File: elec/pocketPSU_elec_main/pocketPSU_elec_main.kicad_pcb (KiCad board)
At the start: 2 copper layers, 90 x 90 mm, 72 parts, among them J1 Conn_01x20_Pin, J2 Conn_01x03_Pin, J3 Conn_01x12_Pin, SW1 EC11E09244BS, SW3 TS-1187A-B-A-B, SW6 TS-1187A-B-A-B, U1 2N7002_C5224215, U2 ESP32-S3-WROOM-1(N16R2), U3 AMS1117-3.3, U4 FUSB302MPX, U5 F.0603.00026/P2-0603B1TS2-06T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

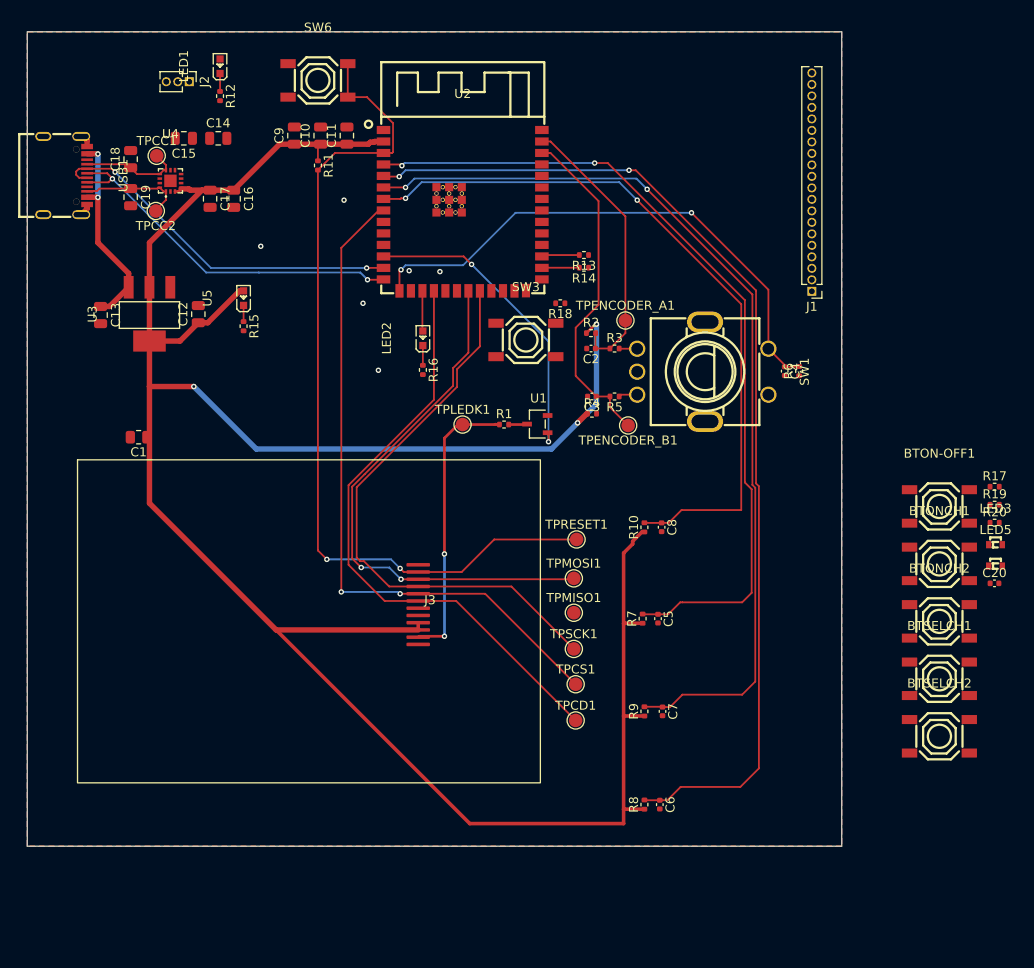
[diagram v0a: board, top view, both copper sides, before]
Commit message: move components, add mounting holes
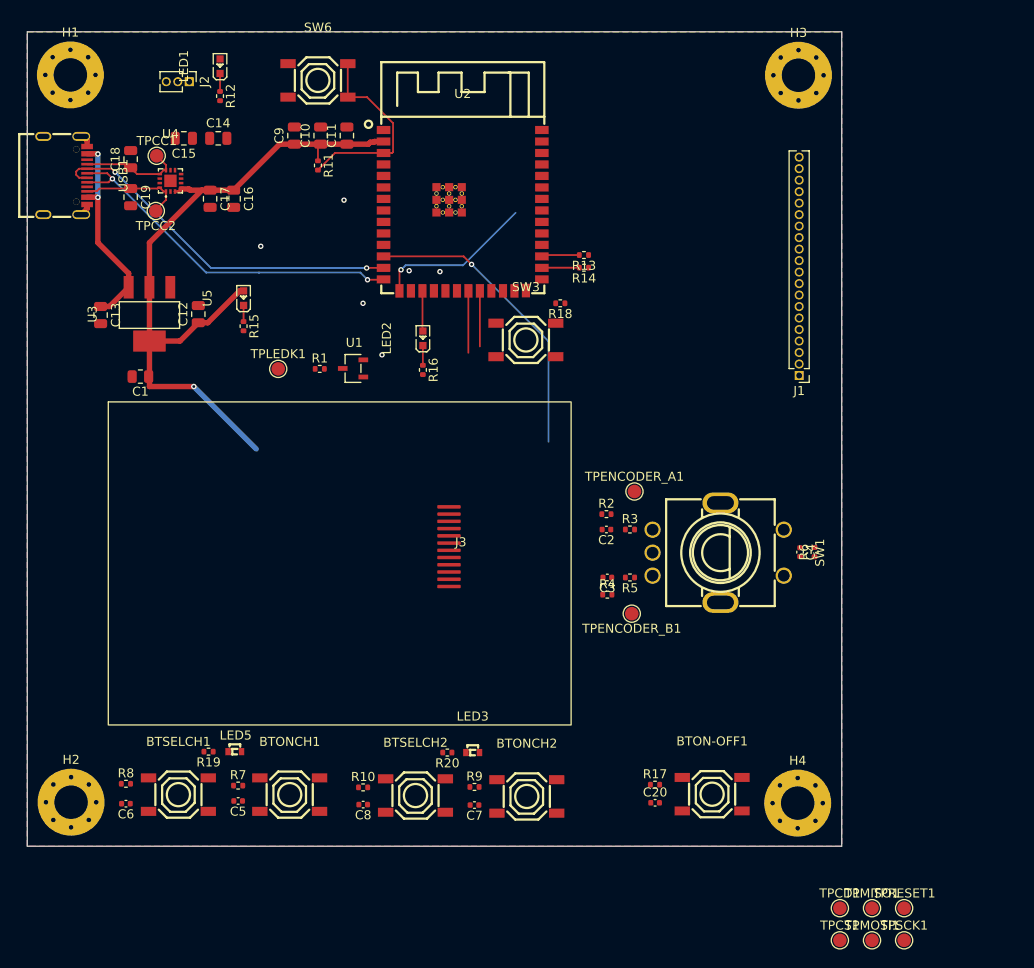
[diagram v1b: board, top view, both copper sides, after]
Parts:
- added H1: MountingHole, MountingHole:MountingHole_3.7mm_Pad_Via, F.Cu at (102.4, 40.5)
- added H2: MountingHole, MountingHole:MountingHole_3.7mm_Pad_Via, F.Cu at (102.4, 120.8)
- added H3: MountingHole, MountingHole:MountingHole_3.7mm_Pad_Via, F.Cu at (182.8, 40.5)
- added H4: MountingHole, MountingHole:MountingHole_3.7mm_Pad_Via, F.Cu at (182.7, 120.9)
- moved R19 91.1 mm to (117.6, 115.2), turned to 180 degrees
- moved LED5 86.5 mm to (120.5, 115.2)
- moved BTSELCH1 85.1 mm to (114.3, 120.0)
- moved BTONCH1 76.2 mm to (126.6, 120.0)
- moved R20 65.6 mm to (144.0, 115.3), turned to 180 degrees
- moved LED3 62.2 mm to (146.8, 115.3)
- moved C6 59.0 mm to (108.5, 121.0), turned to 180 degrees
- moved BTSELCH2 58.3 mm to (140.5, 120.1)
- moved R8 57.3 mm to (108.5, 118.8), turned to 0 degrees
- moved TPRESET1 54.5 mm to (194.5, 132.6)
- moved TPMOSI1 51.8 mm to (190.9, 136.1)
- moved C5 50.6 mm to (120.9, 120.7), turned to 180 degrees
- moved R17 49.9 mm to (167.0, 118.9)
- moved BTONCH2 49.5 mm to (152.8, 120.2)
- moved TPSCK1 48.7 mm to (194.5, 136.1)
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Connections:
- BTON-OFF1 pad 1: /microcontroller/BT_ON_CH2 -> /microcontroller/BT_ON_OFF
- BTON-OFF1 pad 2: /microcontroller/BT_ON_CH2 -> /microcontroller/BT_ON_OFF
- BTSELCH1 pad 1: /microcontroller/BT_ON_OFF -> /microcontroller/BT_ON_CH2
- BTSELCH1 pad 2: /microcontroller/BT_ON_OFF -> /microcontroller/BT_ON_CH2
- C20 pad 1: /microcontroller/BT_ON_CH2 -> /microcontroller/BT_ON_OFF
- C6 pad 1: /microcontroller/BT_ON_OFF -> /microcontroller/BT_ON_CH2
- R17 pad 2: /microcontroller/BT_ON_CH2 -> /microcontroller/BT_ON_OFF
- R8 pad 2: /microcontroller/BT_ON_OFF -> /microcontroller/BT_ON_CH2
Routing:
- net (no net): track 194.0 -> 0.00 mm, vias 4 -> 0
- net +3.3V: track 266.9 -> 78.9 mm, vias 3 -> 1
- net /microcontroller/BT_SEL_CH2: track 102.8 -> 0.00 mm, vias 2 -> 0
- net /microcontroller/BT_SEL_CH1: track 92.1 -> 0.00 mm, vias 2 -> 0
- net /user_interface/SPI_CS: track 74.5 -> 0.53 mm, vias 2 -> 0
- net /user_interface/SPI_RESET: track 95.3 -> 22.2 mm, vias 2 -> 0
- net /user_interface/SPI_DC: track 66.4 -> 0.00 mm
- net /user_interface/SPI_SCK: track 63.3 -> 6.14 mm
- net /user_interface/SPI_MOSI: track 60.4 -> 6.84 mm, vias 2 -> 0
- net /microcontroller/ENCODER_BT: track 60.0 -> 17.7 mm, vias 2 -> 1
- net /microcontroller/ENCODER_B: track 37.6 -> 0.00 mm
- net /user_interface/LEDK: track 31.6 -> 0.00 mm, vias 2 -> 0
- net /microcontroller/ENCODER_A: track 31.3 -> 0.00 mm
- net Net-(R5-Pad1): track 2.07 -> 0.00 mm
- net Net-(R3-Pad2): track 2.00 -> 0.00 mm
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
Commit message: board routed
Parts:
- J1: value Conn_01x20_Pin -> Header-Male-2.54_1x20; footprint Connector_PinHeader_1.27mm:PinHeader_1x20_P1.27mm_Vertical -> footprints:HDR-TH_20P-P2.54-V-M-1
- moved TPMISO1 79.3 mm to (144.9, 68.0)
- moved TPRESET1 61.4 mm to (160.1, 81.7)
- moved TPMOSI1 59.6 mm to (160.1, 85.1)
- moved TPSCK1 58.8 mm to (160.0, 88.5)
- moved TPCS1 51.9 mm to (159.9, 92.1)
- moved TPCD1 45.9 mm to (160.0, 95.7)
- moved R6 18.6 mm to (170.1, 104.8), turned to 0 degrees
- moved C4 16.4 mm to (170.1, 103.2), turned to 180 degrees
- moved R4 16.4 mm to (165.4, 82.0), turned to -90 degrees
- moved TPENCODER_B1 15.4 mm to (163.3, 84.7), turned to 90 degrees
- moved C3 15.1 mm to (167.3, 82.0), turned to 90 degrees
- moved R2 14.5 mm to (174.3, 81.8), turned to -90 degrees
- moved C2 14.1 mm to (172.6, 81.8), turned to 90 degrees
- moved TPENCODER_A1 12.2 mm to (176.8, 85.0), turned to -90 degrees
- moved R5 11.9 mm to (167.3, 84.5), turned to 90 degrees
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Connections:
- J1 pad 1: /microcontroller/IO17 -> unconnected-(J1-Pad1)
- J1 pad 10: /microcontroller/IO45 -> /microcontroller/IO46
- J1 pad 11: /microcontroller/IO46 -> /microcontroller/IO45
- J1 pad 12: /microcontroller/IO47 -> /microcontroller/IO42
- J1 pad 13: /microcontroller/IO48 -> /microcontroller/IO41
- J1 pad 14: /microcontroller/TXD0 -> /microcontroller/IO40
- J1 pad 15: /microcontroller/RXD0 -> /microcontroller/IO39
- J1 pad 16: unconnected-(J1-Pin_16-Pad16) -> /microcontroller/IO38
- J1 pad 17: unconnected-(J1-Pin_17-Pad17) -> /microcontroller/IO21
- J1 pad 18: unconnected-(J1-Pin_18-Pad18) -> /microcontroller/IO11
- J1 pad 19: unconnected-(J1-Pin_19-Pad19) -> /microcontroller/IO18
- J1 pad 2: /microcontroller/IO18 -> unconnected-(J1-Pad2)
- J1 pad 20: unconnected-(J1-Pin_20-Pad20) -> /microcontroller/IO17
- J1 pad 3: /microcontroller/IO11 -> unconnected-(J1-Pad3)
- J1 pad 4: /microcontroller/IO21 -> unconnected-(J1-Pad4)
- J1 pad 5: /microcontroller/IO38 -> unconnected-(J1-Pad5)
- J1 pad 6: /microcontroller/IO39 -> /microcontroller/RXD0
- J1 pad 7: /microcontroller/IO40 -> /microcontroller/TXD0
- J1 pad 8: /microcontroller/IO41 -> /microcontroller/IO48
- J1 pad 9: /microcontroller/IO42 -> /microcontroller/IO47
- R18 pad 2: Net-(SW3-B) -> Net-(SW3-A)
- R2 pad 2: /microcontroller/ENCODER_A -> Net-(R2-Pad2)
- R3 pad 2: Net-(R3-Pad2) -> Net-(R2-Pad2)
- R4 pad 2: /microcontroller/ENCODER_B -> Net-(R4-Pad2)
- R5 pad 1: Net-(R5-Pad1) -> Net-(R4-Pad2)
- SW1 pad A: Net-(R3-Pad2) -> Net-(R2-Pad2)
- SW1 pad B: Net-(R5-Pad1) -> Net-(R4-Pad2)
- SW3 pad 1: GND -> Net-(SW3-A)
- SW3 pad 2: Net-(SW3-B) -> Net-(SW3-A)
- SW3 pad 4: Net-(SW3-B) -> GND
- SW6 pad 1: GND -> /user_interface/SPI_RESET
- SW6 pad 4: /user_interface/SPI_RESET -> GND
- U2 pad 27: Net-(SW3-B) -> Net-(SW3-A)
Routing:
- net +3.3V: track 78.9 -> 305.3 mm, vias 1 -> 10
- net /microcontroller/BT_ON_OFF: track 0.00 -> 106.7 mm, vias 0 -> 2
- net /user_interface/SPI_RESET: track 22.2 -> 118.2 mm, vias 0 -> 7
- net /microcontroller/BT_SEL_CH2: track 0.00 -> 93.7 mm
- net /microcontroller/BT_ON_CH2: track 0.00 -> 91.4 mm, vias 0 -> 2
- net /microcontroller/BT_ON_CH1: track 0.00 -> 88.3 mm
- net /microcontroller/BT_SEL_CH1: track 0.00 -> 87.0 mm
- net /microcontroller/CH2_LED: track 0.00 -> 76.0 mm, vias 0 -> 2
- net /user_interface/SPI_CS: track 0.53 -> 70.6 mm, vias 0 -> 6
- net /microcontroller/CH1_LED: track 0.00 -> 69.0 mm, vias 0 -> 2
- net /microcontroller/IO11: track 0.00 -> 65.5 mm, vias 0 -> 1
- net /microcontroller/ENCODER_A: track 0.00 -> 65.0 mm, vias 0 -> 2
- net /microcontroller/IO21: track 0.00 -> 61.5 mm, vias 0 -> 3
- net /microcontroller/ENCODER_B: track 0.00 -> 58.6 mm, vias 0 -> 2
- net /microcontroller/IO46: track 0.00 -> 57.5 mm, vias 0 -> 3
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
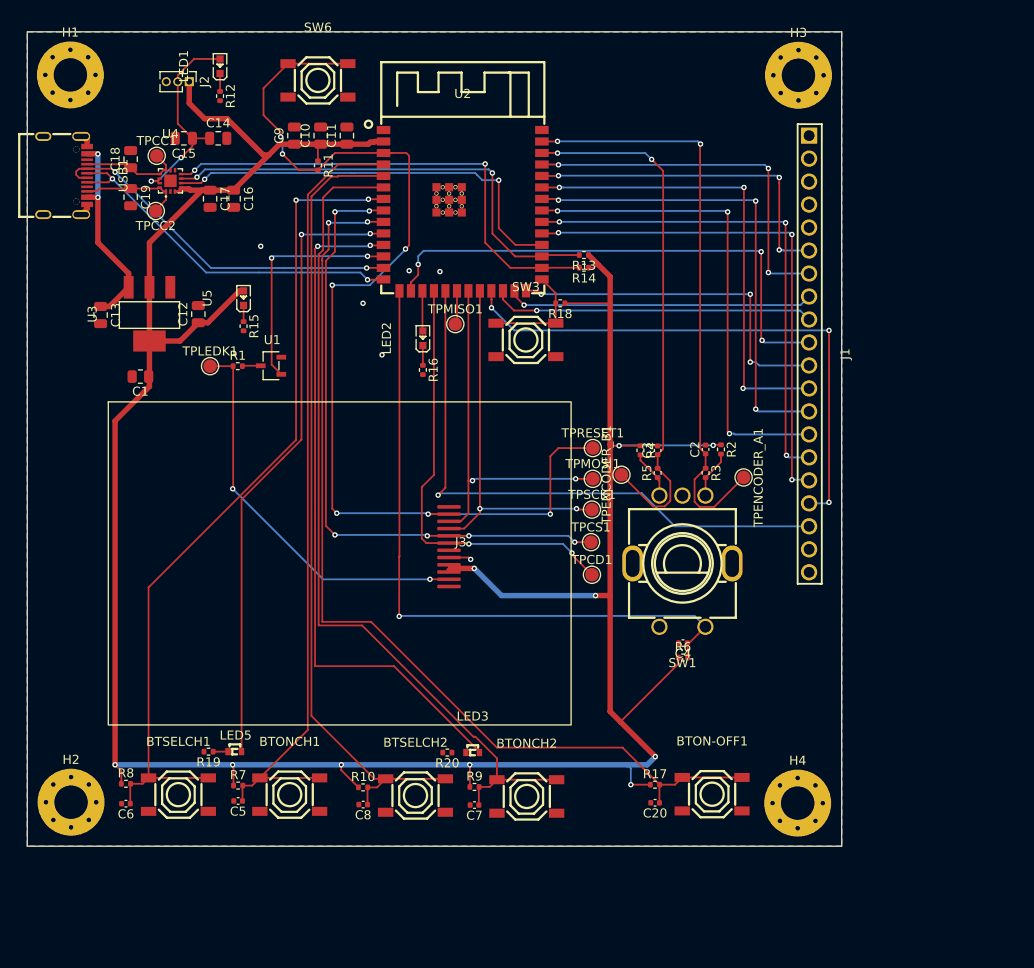
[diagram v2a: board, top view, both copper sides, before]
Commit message: add groud vias
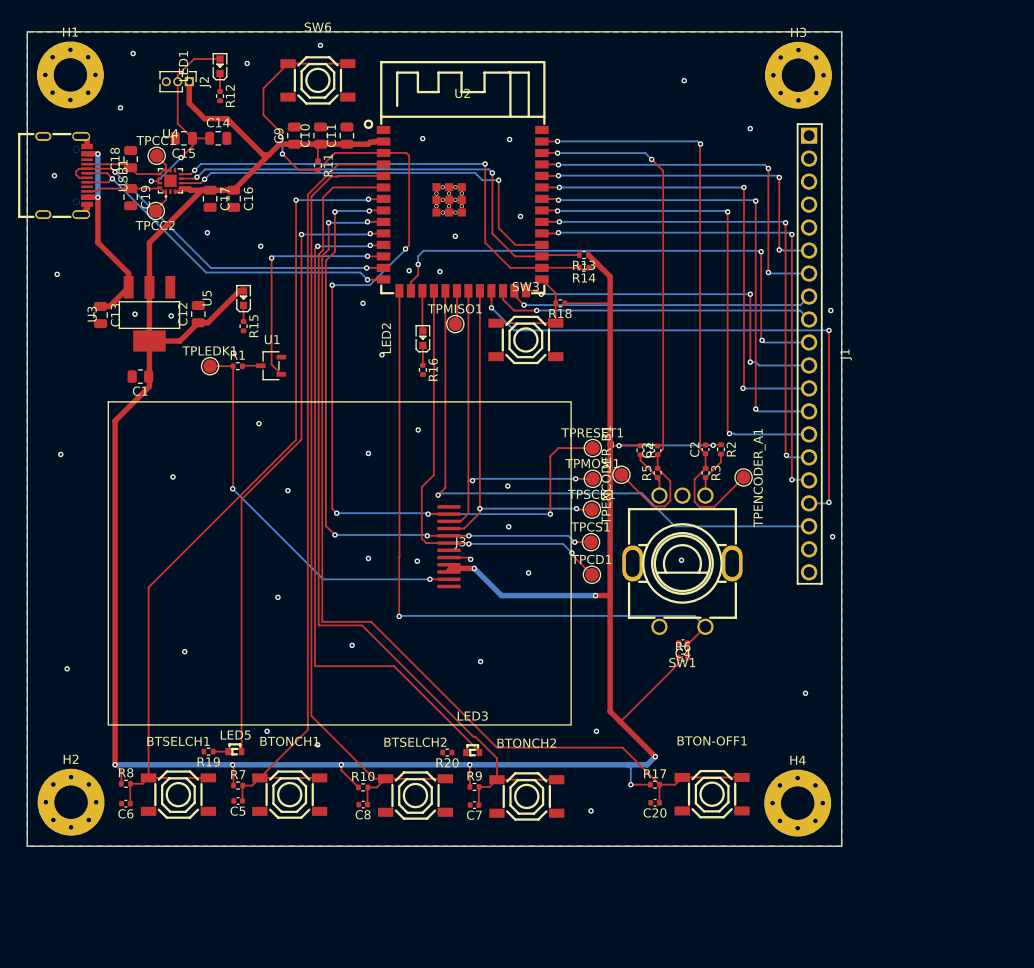
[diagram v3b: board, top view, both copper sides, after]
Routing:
- net GND: vias 6 -> 45

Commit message: fix some drcs
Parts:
- moved TPCC1 4.49 mm to (110.3, 45.2)
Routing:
- net /usb_input/USB_CC1: track 11.4 -> 16.2 mm
- net GND: track 5.08 -> 9.21 mm, vias 45 -> 53
- net /microcontroller/ENCODER_A: track 65.0 -> 66.9 mm
- net /microcontroller/ENCODER_B: track 58.6 -> 59.6 mm
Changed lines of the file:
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@@
 	(footprint "TestPoint:TestPoint_Pad_D1.5mm"
 		(layer "F.Cu")
-		(at 111.9 49.4)
+		(at 110.3 45.2)
 		(descr "SMD pad as test Point, diameter 1.5mm")
 		(tags "test point SMD pad")
@@
 	)
 	(segment
-		(start 123.668232 49.3)
-		(end 119.668232 45.3)
-		(width 0.6)
-		(layer "F.Cu")
-		(net 1)
-	)
-	(segment
 		(start 120.4 53.2)
 		(end 117.8 53.2)
@@
 	)
 	(segment
+		(start 124.3 49.3)
+		(end 124.3 48.7)
+		(width 0.6)
+		(layer "F.Cu")
+		(net 1)
+	)
+	(segment
 		(start 162.01 65.8)
 		(end 162.01 62.75)
@@
 	)
 	(segment
+		(start 124.3 48.7)
+		(end 120.9 45.3)
+		(width 0.6)
+		(layer "F.Cu")
+		(net 1)
+	)
+	(segment
 		(start 157.01 65.7)
 		(end 161.91 65.7)
@@
 	)
 	(segment
-		(start 124.3 49.3)
-		(end 123.668232 49.3)
-		(width 0.6)
-		(layer "F.Cu")
-		(net 1)
-	)
-	(segment
 		(start 134.2 119.2)
 		(end 132.3 117.3)
@@
 	)
 	(segment
-		(start 117.2 45.3)
-		(end 115.5 43.6)
+		(start 125.4825 48.1175)
+		(end 124.3 49.3)
 		(width 0.6)
 		(layer "F.Cu")
@@
 	)
 	(segment
-		(start 125.4825 48.1175)
-		(end 124.3 49.3)
+		(start 120.9 45.3)
+		(end 117.2 45.3)
 		(width 0.6)
 		(layer "F.Cu")
@@
 	)
 	(segment
+		(start 115.5 43.6)
+		(end 115.5 41.21)
+		(width 0.6)
+		(layer "F.Cu")
+		(net 1)
+	)
+	(segment
+		(start 117.2 45.3)
+		(end 115.5 43.6)
+		(width 0.6)
+		(layer "F.Cu")
+		(net 1)
+	)
+	(segment
 		(start 115.46 53.06)
 		(end 114.6 53.06)
@@
 	)
 	(segment
-		(start 119.668232 45.3)
-		(end 117.2 45.3)
-		(width 0.6)
-		(layer "F.Cu")
-		(net 1)
-	)
-	(segment
 		(start 162.01 81.3)
 		(end 162.01 65.8)
@@
 	)
 	(segment
-		(start 115.5 43.6)
-		(end 115.5 41.21)
-		(width 0.6)
-		(layer "F.Cu")
-		(net 1)
-	)
-	(segment
 		(start 146.51 119.15)
 		(end 146.51 116.71)
@@
 	)
 	(segment
+		(start 142.6 88.2)
+		(end 144.2 88.2)
+		(width 0.2)
+		(layer "F.Cu")
+		(net 2)
+	)
+	(segment
+		(start 142 87.6)
+		(end 142.6 88.2)
+		(width 0.2)
+		(layer "F.Cu")
+		(net 2)
+	)
+	(segment
 		(start 103.76 47.26)
 		(end 104.2075 47.7075)
@@
 	)
 	(segment
+		(start 113.42 50.99)
+		(end 113.42 52.17)
+		(width 0.2)
+		(layer "F.Cu")
+		(net 2)
+	)
+	(segment
 		(start 144.2 93.7975)
 		(end 146.3975 93.7975)
@@
 	)
 	(segment
+		(start 113.42 50.99)
+		(end 113.92 50.99)
+		(width 0.2)
+		(layer "F.Cu")
+		(net 2)
+	)
+	(segment
 		(start 104.2075 55.25)
 		(end 103.5575 55.9)
@@
 	)
 	(via
+		(at 121.8 48.7)
+		(size 0.6)
+		(drill 0.3)
+		(layers "F.Cu" "B.Cu")
+		(free yes)
+		(net 2)
+	)
+	(via
 		(at 102 106.1)
 		(size 0.6)
@@
 	)
 	(via
+		(at 116.8 49.2)
+		(size 0.6)
+		(drill 0.3)
+		(layers "F.Cu" "B.Cu")
+		(free yes)
+		(net 2)
+	)
+	(via
+		(at 122.4 44.6)
+		(size 0.6)
+		(drill 0.3)
+		(layers "F.Cu" "B.Cu")
+		(free yes)
+		(net 2)
+	)
+	(via
 		(at 113.5 67.1)
 		(size 0.6)
@@
 	)
 	(via
+		(at 169.4 62.4)
+		(size 0.6)
+		(drill 0.3)
+		(layers "F.Cu" "B.Cu")
+		(free yes)
+		(net 2)
+	)
+	(via
 		(at 177.5 46.4)
 		(size 0.6)
@@
 	)
 	(via
+		(at 142 87.6)
+		(size 0.6)
+		(drill 0.3)
+		(layers "F.Cu" "B.Cu")
+		(free yes)
+		(net 2)
+	)
+	(via
 		(at 140.8 79.7)
 		(size 0.6)
@@
 	)
 	(via
+		(at 113.4 52.2)
+		(size 0.6)
+		(drill 0.3)
+		(layers "F.Cu" "B.Cu")
+		(net 2)
+	)
+	(via
 		(at 150.7 85.9)
 		(size 0.6)
@@
 	)
 	(via
+		(at 169.4 77.2)
+		(size 0.6)
+		(drill 0.3)
+		(layers "F.Cu" "B.Cu")
+		(free yes)
+		(net 2)
+	)
+	(via
 		(at 136.8 71.4)
 		(size 0.6)
@@
 		(net 2)
 	)
+	(via
+		(at 168.8 49.2)
+		(size 0.6)
+		(drill 0.3)
+		(layers "F.Cu" "B.Cu")
+		(free yes)
+		(net 2)
+	)
 	(segment
 		(start 142.1 96.2)
@@
 	)
 	(segment
-		(start 171.95 81.72)
-		(end 172.56 82.33)
-		(width 0.2)
-		(layer "F.Cu")
-		(net 10)
-	)
-	(segment
 		(start 171.34 85.16)
 		(end 171.34 87.64)
@@
 	)
 	(segment
+		(start 172 48.1)
+		(end 170.3 49.8)
+		(width 0.2)
+		(layer "F.Cu")
+		(net 10)
+	)
+	(segment
 		(start 172.56 83.94)
 		(end 171.34 85.16)
@@
 	)
 	(segment
-		(start 171.95 48.15)
-		(end 171.95 81.72)
+		(start 171.63 82.33)
+		(end 172.56 82.33)
 		(width 0.2)
 		(layer "F.Cu")
@@
 	)
 	(segment
-		(start 171.34 87.64)
-		(end 171.9 88.2)
+		(start 170.3 49.8)
+		(end 170.3 81)
 		(width 0.2)
 		(layer "F.Cu")
@@
 	)
 	(segment
-		(start 172 48.1)
-		(end 171.95 48.15)
+		(start 170.3 81)
+		(end 171.63 82.33)
+		(width 0.2)
+		(layer "F.Cu")
+		(net 10)
+	)
+	(segment
+		(start 171.34 87.64)
+		(end 171.9 88.2)
 		(width 0.2)
 		(layer "F.Cu")
@@
 	)
 	(segment
-		(start 167.87 81.82)
+		(start 166.6 49.8)
+		(end 168.6 51.8)
+		(width 0.2)
+		(layer "F.Cu")
+		(net 11)
+	)
+	(segment
+		(start 168.6 51.8)
+		(end 168.6 81.8)
+		(width 0.2)
+		(layer "F.Cu")
+		(net 11)
+	)
+	(segment
+		(start 167.97 82.43)
 		(end 167.26 82.43)
 		(width 0.2)
@@
 	)
 	(segment
-		(start 167.87 51.07)
-		(end 167.87 81.82)
+		(start 168.6 81.8)
+		(end 167.97 82.43)
 		(width 0.2)
 		(layer "F.Cu")
@@
 		(net 11)
 	)
-	(segment
-		(start 166.6 49.8)
-		(end 167.87 51.07)
-		(width 0.2)
-		(layer "F.Cu")
-		(net 11)
-	)
 	(via
 		(at 156.2 49.1)
@@
 	)
 	(segment
-		(start 111.9 49.4)
-		(end 112.92 50.42)
+		(start 112.92 50.99)
+		(end 112.6 50.67)
+		(width 0.2)
+		(layer "F.Cu")
+		(net 18)
+	)
+	(segment
+		(start 112.6 49.6)
+		(end 110.3 47.3)
 		(width 0.2)
 		(layer "F.Cu")
@@
 	)
 	(segment
+		(start 110.3 47.3)
+		(end 110.3 45.2)
+		(width 0.2)
+		(layer "F.Cu")
+		(net 18)
+	)
+	(segment
 		(start 109.72 51.42)
 		(end 109.02 50.72)
@@
 	)
 	(segment
-		(start 112.67 50.99)
-		(end 112.92 50.99)
+		(start 112.6 50.67)
+		(end 112.6 49.6)
 		(width 0.2)
 		(layer "F.Cu")
@@
 	)
 	(segment
-		(start 112.92 50.42)
+		(start 112.67 50.99)
 		(end 112.92 50.99)
 		(width 0.2)
